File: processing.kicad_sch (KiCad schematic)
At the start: 45 parts, among them IC10 MT29F2G01ABAGDWB-IT_G_TR, IC2 XMC7200D-E272K8384AA, IC6 DS90LV011AHMF_NOPB, IC9 MT29F2G01ABAGDWB-IT_G_TR, Q1 ZXT849K, Y1 DSC1101DM2-012.0000

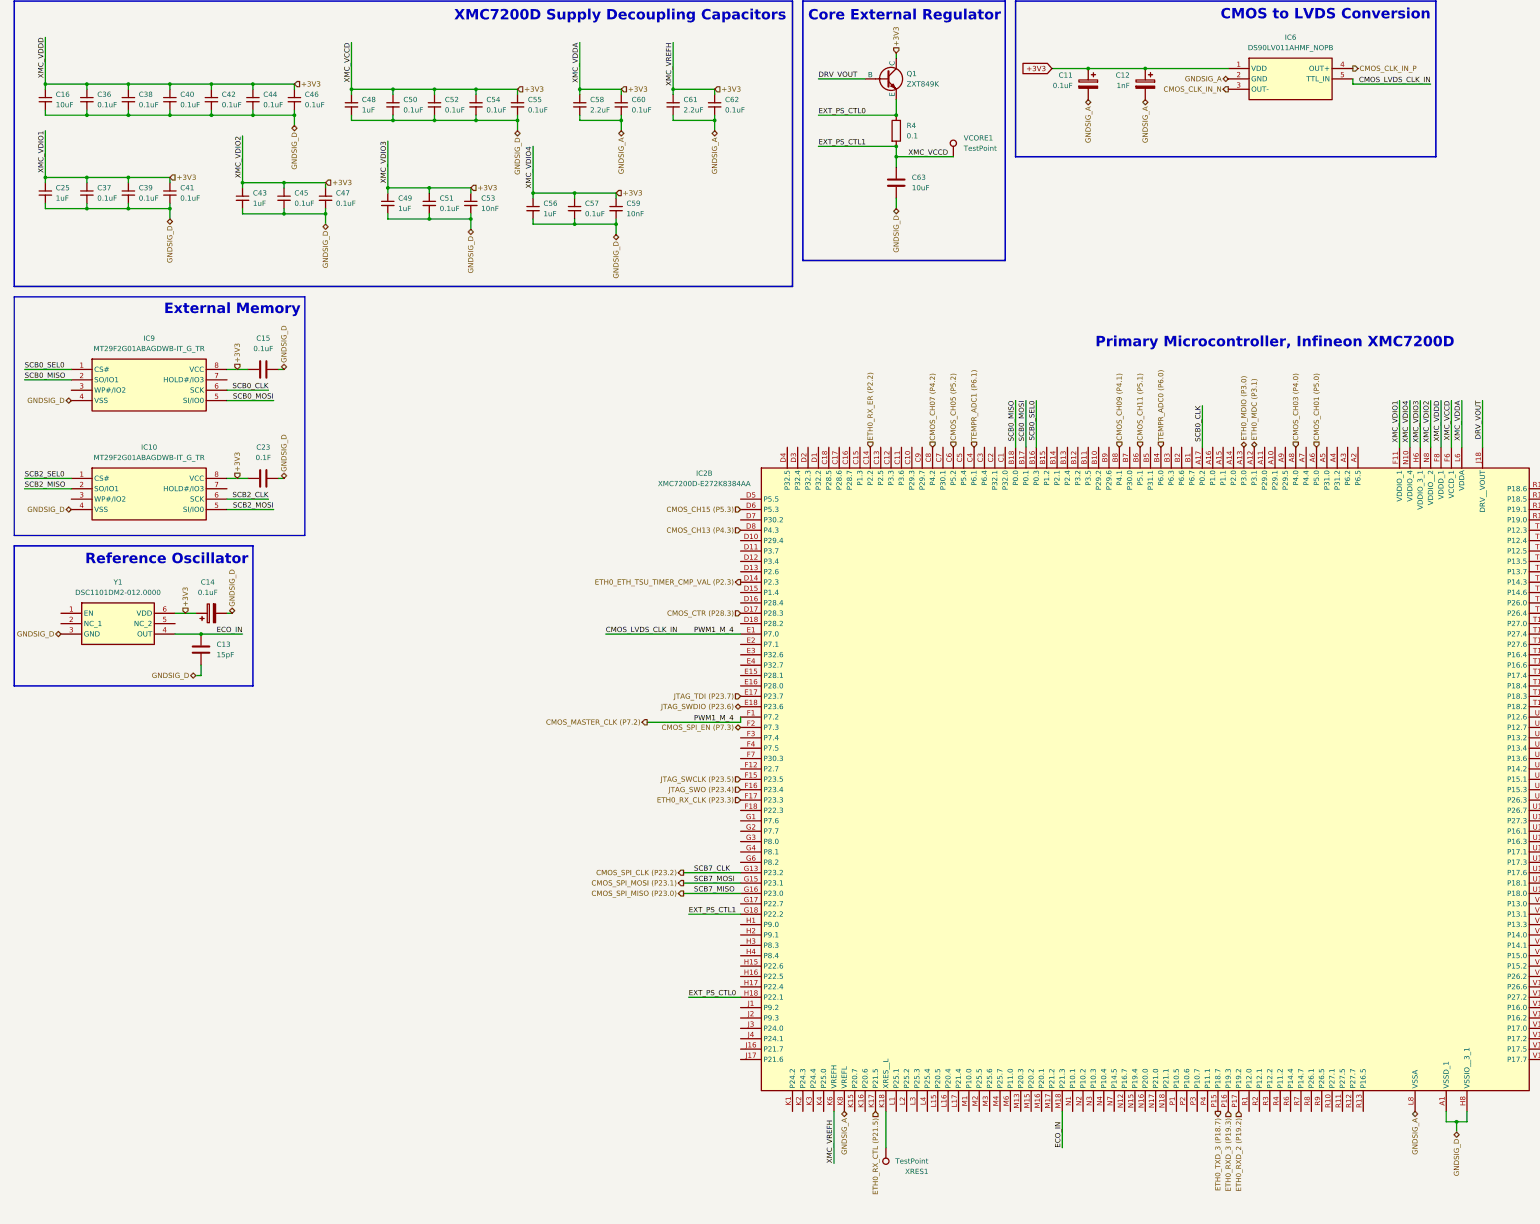
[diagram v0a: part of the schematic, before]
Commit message: One gnd to rule them all; PCB border (90 mm x 90 mm)
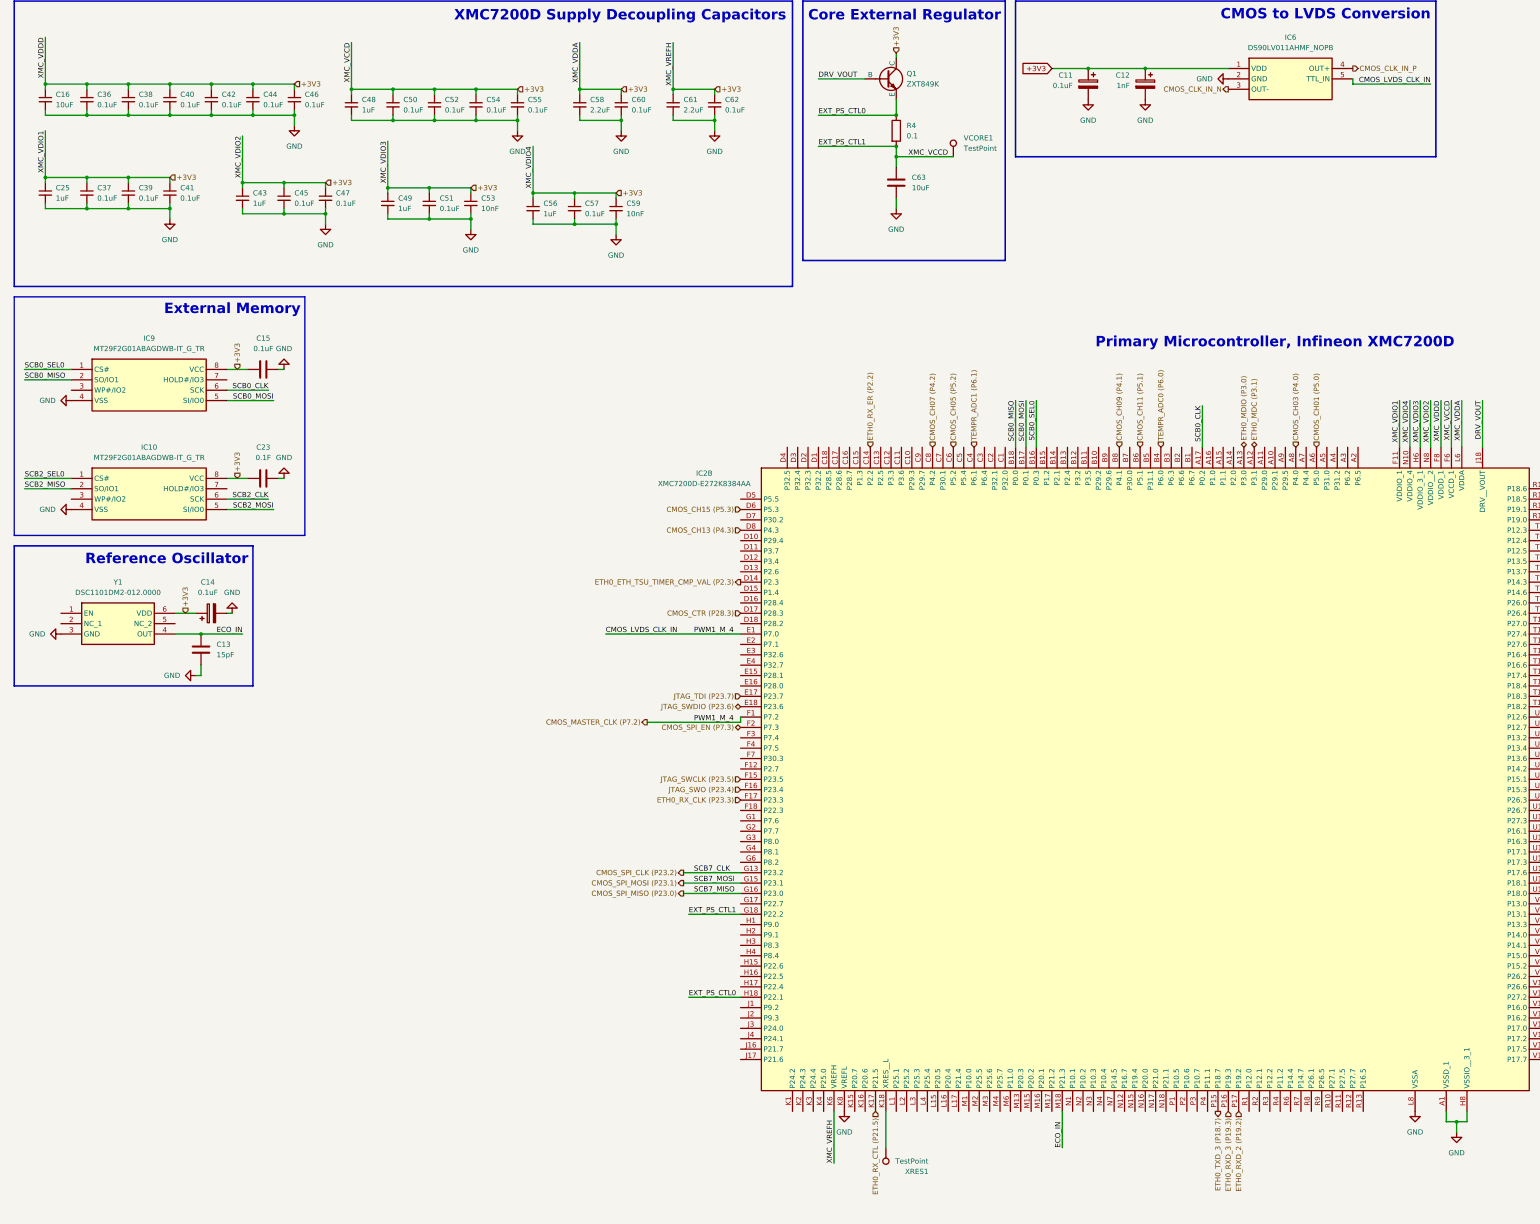
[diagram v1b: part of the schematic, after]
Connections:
- net GNDSIG_D is gone; now on net GND: C13.2, C14.2, C15.2, C16.2, C23.2, C25.2, C36.2, C37.2, C38.2, C39.2, C40.2, C41.2, C42.2, C43.2, C44.2, C45.2, C46.2, C47.2, C48.2, C49.2, C50.2, C51.2, C52.2, C53.2, C54.2, C55.2, C56.2, C57.2, C59.2, C63.2, IC10.4 (VSS), IC2.A1 (VSSD_1), IC2.A18 (VSSD_2), IC2.D9 (VSSD_3), IC2.G12 (VSSD_5), IC2.G7 (VSSD_4), IC2.H10 (VSSD_7), IC2.H11 (VSSD_8), IC2.H8 (VSSIO__3_1), IC2.H9 (VSSD_6), IC2.J10 (VSSD_10), IC2.J11 (VSSD_11), IC2.J15 (VSSD_12), IC2.J8 (VSSIO__3_2), IC2.J9 (VSSD_9), IC2.K10 (VSSD_14), IC2.K11 (VSSD_15), IC2.K9 (VSSD_13), IC2.L10 (VSSIO__4_2), IC2.L11 (VSSD__1), IC2.L18 (VSSD__2_1), IC2.L9 (VSSIO__4_1), IC2.M12 (VSSD_17), IC2.M7 (VSSD_16), IC2.P18 (VSSD__2_2), IC2.R14 (VSSD_19), IC2.R5 (VSSD_18), IC2.V1 (VSSD_20), IC2.V18 (VSSD_21), IC9.4 (VSS), Y1.3 (GND)
- net GNDSIG_A renamed GND

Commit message: 3v3 Regulator routed; zones for 3v3 and gnd
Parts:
- IC10, IC9: footprint SON127P800X600X65-8N -> SamacSys_Parts:SON127P800X600X65-8N
- IC2: footprint BGA272C80P18X18_1600X1600X170 -> SamacSys_Parts:BGA272C80P18X18_1600X1600X170
- IC6: footprint SOT95P280X145-5N -> SamacSys_Parts:SOT95P280X145-5N
- Y1: footprint DSC1101DM20120000 -> SamacSys_Parts:DSC1101DM20120000
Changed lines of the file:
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@@
 			)
 		)
-		(property "Footprint" "SON127P800X600X65-8N"
+		(property "Footprint" "SamacSys_Parts:SON127P800X600X65-8N"
 			(at 62.23 199.06 0)
 			(effects
@@
 			)
 		)
-		(property "Footprint" "BGA272C80P18X18_1600X1600X170"
+		(property "Footprint" "SamacSys_Parts:BGA272C80P18X18_1600X1600X170"
 			(at 257.81 200.33 0)
 			(effects
@@
 			)
 		)
-		(property "Footprint" "DSC1101DM20120000"
+		(property "Footprint" "SamacSys_Parts:DSC1101DM20120000"
 			(at 49.53 258.75 0)
 			(effects
@@
 			)
 		)
-		(property "Footprint" "SON127P800X600X65-8N"
+		(property "Footprint" "SamacSys_Parts:SON127P800X600X65-8N"
 			(at 62.23 225.73 0)
 			(effects
@@
 			)
 		)
-		(property "Footprint" "SOT95P280X145-5N"
+		(property "Footprint" "SamacSys_Parts:SOT95P280X145-5N"
 			(at 337.82 125.4 0)
 			(effects

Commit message: Schematic - Component Specifics
Fixed floating connections.
Added parameters, footprints, Mouser part numbers, and Mouser links to all symbols, including discrete components and ICs.
The following symbols do not have Mouser part numbers or Mouser links:
CMOS Sensor (not required)
RJ45 Connector
JTAG Connector
DC Barrel Jack
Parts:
- removed C12: 1nF, symbol Device:C_Polarized
- removed C15: 0.1uF, symbol Device:C
- removed C23: 0.1F, symbol Device:C
- removed C47: 0.1uF, symbol Device:C_Small
- removed C56: 1uF, symbol Device:C_Small
- removed C63: 10uF, symbol Device:C
- added C12: 1nF, Capacitor_SMD:C_0603_1608Metric, symbol Device:C_Small
- added C15, C23: 0.1uF, Capacitor_SMD:C_0603_1608Metric, symbol Device:C_Small
- added C33: 10uF, Capacitor_SMD:C_0603_1608Metric, symbol Device:C_Small
- added C69: 10nF, Capacitor_SMD:C_0603_1608Metric, symbol Device:C_Small
- added C71: 1uF, Capacitor_SMD:C_0603_1608Metric, symbol Device:C_Small
- added R5, R6: 10k, Resistor_SMD:R_0603_1608Metric, symbol Device:R
- C11, C14: footprint (none) -> Capacitor_SMD:C_0805_2012Metric; Dielectric (none) -> TANT; Mouser Part Number (none) -> 581-TAJR104K020R; Mouser Price/Stock (none) -> https://www.mouser.com/ProductDetail/KYOCERA-AVX/TAJR104K02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; Tolerance (none) -> 10%; Voltage Rating (none) -> 20V
- C13: Dielectric (none) -> X7R; Mouser Part Number (none) -> 80-C0603C150J5RACTU; Mouser Price/Stock (none) -> https://www.mouser.com/ProductDetail/KEMET/C0603C150J5RACTU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; Tolerance (none) -> 5%; Voltage Rating (none) -> 50V
- C16: footprint (none) -> Capacitor_SMD:C_0603_1608Metric; Dielectric (none) -> X7R; Mouser Part Number (none) -> 81-GRM188Z71A106MA3J; Mouser Price/Stock (none) -> https://www.mouser.com/ProductDetail/Murata-Electronics/GRM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; Tolerance (none) -> 20%; Voltage Rating (none) -> 10V
- C25, C43, C48, C49: footprint (none) -> Capacitor_SMD:C_0603_1608Metric; Dielectric (none) -> X7R; Mouser Part Number (none) -> 963-MLASU168AB7105KT; Mouser Price/Stock (none) -> https://www.mouser.com/ProductDetail/TAIYO-YUDEN/MLASU168AB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; Tolerance (none) -> 10%; Voltage Rating (none) -> 50V
- C36, C37, C38, C39, C40, C41, C42, C44, C45, C46, C50, C51, C52, C54, C55, C57, C60, C62: footprint (none) -> Capacitor_SMD:C_0603_1608Metric; Dielectric (none) -> X7R; Mouser Part Number (none) -> 81-GCM188R71C104KA7J; Mouser Price/Stock (none) -> https://www.mouser.com/ProductDetail/Murata-Electronics/GCM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; Tolerance (none) -> 10%; Voltage Rating (none) -> 16V
- C53: footprint (none) -> Capacitor_SMD:C_0603_1608Metric; Dielectric (none) -> X7R; Mouser Part Number (none) -> 81-GCM188R71H103KA7J; Mouser Price/Stock (none) -> https://www.mouser.com/ProductDetail/Murata-Electronics/GCM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; Tolerance (none) -> 10%; Voltage Rating (none) -> 50V
- C58, C61: footprint (none) -> Capacitor_SMD:C_0603_1608Metric; Dielectric (none) -> X7R; Mouser Part Number (none) -> 963-LMK107B7225KA-TR; Mouser Price/Stock (none) -> https://www.mouser.com/ProductDetail/TAIYO-YUDEN/LMK107B722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; Tolerance (none) -> 10%; Voltage Rating (none) -> 10V
- C59: value 10nF -> 0.1uF; footprint (none) -> Capacitor_SMD:C_0603_1608Metric; Dielectric (none) -> X7R; Mouser Part Number (none) -> 81-GCM188R71C104KA7J; Mouser Price/Stock (none) -> https://www.mouser.com/ProductDetail/Murata-Electronics/GCM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; Tolerance (none) -> 10%; Voltage Rating (none) -> 16V
- IC10, IC9: Arrow Part Number MT29F2G01ABAGDWB-IT:G TR -> (none); Arrow Price/Stock https://www.arrow.com/en/products/mt29f2g01abagdwb-itg-tr/m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 -> (none); Mouser Part Number (none) -> 340-319922-REEL; Mouser Price/Stock (none) -> https://www.mouser.com/ProductDetail/Micron/MT29F2G01ABAGDW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
- IC2: Mouser Part Number (none) -> 726-C7200DE272K8384A; Mouser Price/Stock (none) -> https://www.mouser.com/ProductDetail/Infineon-Technologies/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
- IC6: Arrow Part Number DS90LV011AHMF/NOPB -> (none); Arrow Price/Stock https://www.arrow.com/en/products/ds90lv011ahmfnopb/texas-i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 -> (none); Mouser Part Number (none) -> 926-DS90LV011AHMFNPB; Mouser Price/Stock (none) -> https://www.mouser.com/ProductDetail/Texas-Instruments/DS90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
- Q1: footprint (none) -> Package_TO_SOT_SMD:TO-252-3_TabPin4; Mouser Part Number (none) -> 522-ZXT849KTC; Mouser Price/Stock (none) -> https://www.mouser.com/ProductDetail/Diodes-Incorporated/ZX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
- R4: footprint (none) -> Resistor_SMD:R_0805_2012Metric; Mouser Part Number (none) -> 755-LTR10LEZPJLR10; Mouser Price/Stock (none) -> https://www.mouser.com/ProductDetail/ROHM-Semiconductor/LTR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; Power Rating (none) -> 1W; Tolerance (none) -> 5%
- Y1: Arrow Part Number DSC1101DM2-012.0000 -> (none); Arrow Price/Stock https://www.arrow.com/en/products/dsc1101dm2-012.0000/micro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 -> (none); Mouser Part Number (none) -> 579-DSC1101DM2012; Mouser Price/Stock (none) -> https://www.mouser.com/ProductDetail/Microchip-Technology/D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
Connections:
- net +3V3: now also C12.1, C15.1, C23.1, C33.1, C69.1, C71.1, R5.1, R6.1
- net GND: now also C12.2, C15.2, C23.2, C33.2, C69.2, C71.2
- net CMOS_RESET_N: now reaches IC2.C11 (P3.6)
- net CMOS_RESET_N: now also R6.2
- net FRAME_REQ: now reaches IC2.D11 (P3.7)
- net HRSTN: now reaches IC2.D13 (P2.6)
- net HRSTN: now also R5.2
- net LVDS_REC_EN: now reaches IC2.D5 (P5.5)
- net CMOS_CLK_OUT: now reaches IC2.J3 (P24.0)
- net ETH0_ETH_TSU_TIMER_CMP_VAL (P2.3): no longer names the net of IC2.D14 (P2.3)
- net ETH0_RX_ER (P2.2): no longer names the net of IC2.C14 (P2.2)
- net ETH0_TX_ER (P18.2): no longer names the net of IC2.T18 (P18.2)
- no-connect marks 0 -> 6
